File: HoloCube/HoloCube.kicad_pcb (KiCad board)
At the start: 4 copper layers, 30 x 29 mm, 38 parts, among them J1 ESPProgUART_RX, J2 Conn_01x08_MountingPin, J3 USB_C_Receptacle_USB2.0, J4 Micro_SD_Card, Q1 MMBT3904, U1 ESP32-PICO-D4, U2 LIS2DH12TR, U3 BH1750FVI-TR, U4 XC6209

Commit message: V0.1 FinalVer
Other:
- board text added: "JLCJLCJLCJLC"
- board text added: "KisonHe"
- board text added: "V0.1"
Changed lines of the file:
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@@
       (outputformat 1)
       (mirror false)
-      (drillshape 1)
+      (drillshape 0)
       (scaleselection 1)
-      (outputdirectory "")
+      (outputdirectory "plot/")
     )
   )
@@
     (fp_line (start 3.5 3.5) (end -3.5 3.5) (layer "F.Fab") (width 0.1))
     (fp_line (start -3.5 -2.5) (end -2.5 -3.5) (layer "F.Fab") (width 0.1))
-    (pad "" smd roundrect (at -0.66 -0.66) (size 1.07 1.07) (layers "F.Paste") (roundrect_rratio 0.233645))
-    (pad "" smd roundrect (at -1.98 -0.66) (size 1.07 1.07) (layers "F.Paste") (roundrect_rratio 0.233645))
-    (pad "" smd roundrect (at -0.66 1.98) (size 1.07 1.07) (layers "F.Paste") (roundrect_rratio 0.233645))
-    (pad "" smd roundrect (at 1.98 -1.98) (size 1.07 1.07) (layers "F.Paste") (roundrect_rratio 0.233645))
-    (pad "" smd roundrect (at 0.66 -1.98) (size 1.07 1.07) (layers "F.Paste") (roundrect_rratio 0.233645))
-    (pad "" smd roundrect (at 0.66 0.66) (size 1.07 1.07) (layers "F.Paste") (roundrect_rratio 0.233645))
-    (pad "" smd roundrect (at 1.98 -0.66) (size 1.07 1.07) (layers "F.Paste") (roundrect_rratio 0.233645))
-    (pad "" smd roundrect (at -1.98 0.66) (size 1.07 1.07) (layers "F.Paste") (roundrect_rratio 0.233645))
-    (pad "" smd roundrect (at -1.98 -1.98) (size 1.07 1.07) (layers "F.Paste") (roundrect_rratio 0.233645))
-    (pad "" smd roundrect (at 1.98 0.66) (size 1.07 1.07) (layers "F.Paste") (roundrect_rratio 0.233645))
-    (pad "" smd roundrect (at -1.98 1.98) (size 1.07 1.07) (layers "F.Paste") (roundrect_rratio 0.233645))
-    (pad "" smd roundrect (at -0.66 0.66) (size 1.07 1.07) (layers "F.Paste") (roundrect_rratio 0.233645))
-    (pad "" smd roundrect (at 1.98 1.98) (size 1.07 1.07) (layers "F.Paste") (roundrect_rratio 0.233645))
-    (pad "" smd roundrect (at -0.66 -1.98) (size 1.07 1.07) (layers "F.Paste") (roundrect_rratio 0.233645))
-    (pad "" smd roundrect (at 0.66 -0.66) (size 1.07 1.07) (layers "F.Paste") (roundrect_rratio 0.233645))
-    (pad "" smd roundrect (at 0.66 1.98) (size 1.07 1.07) (layers "F.Paste") (roundrect_rratio 0.233645))
+    (pad "" smd roundrect (at -0.66 -0.66) (size 1.07 1.07) (layers "F.Paste") (roundrect_rratio 0.2336448598))
+    (pad "" smd roundrect (at -1.98 -0.66) (size 1.07 1.07) (layers "F.Paste") (roundrect_rratio 0.2336448598))
+    (pad "" smd roundrect (at -0.66 1.98) (size 1.07 1.07) (layers "F.Paste") (roundrect_rratio 0.2336448598))
+    (pad "" smd roundrect (at 1.98 -1.98) (size 1.07 1.07) (layers "F.Paste") (roundrect_rratio 0.2336448598))
+    (pad "" smd roundrect (at 0.66 -1.98) (size 1.07 1.07) (layers "F.Paste") (roundrect_rratio 0.2336448598))
+    (pad "" smd roundrect (at 0.66 0.66) (size 1.07 1.07) (layers "F.Paste") (roundrect_rratio 0.2336448598))
+    (pad "" smd roundrect (at 1.98 -0.66) (size 1.07 1.07) (layers "F.Paste") (roundrect_rratio 0.2336448598))
+    (pad "" smd roundrect (at -1.98 0.66) (size 1.07 1.07) (layers "F.Paste") (roundrect_rratio 0.2336448598))
+    (pad "" smd roundrect (at -1.98 -1.98) (size 1.07 1.07) (layers "F.Paste") (roundrect_rratio 0.2336448598))
+    (pad "" smd roundrect (at 1.98 0.66) (size 1.07 1.07) (layers "F.Paste") (roundrect_rratio 0.2336448598))
+    (pad "" smd roundrect (at -1.98 1.98) (size 1.07 1.07) (layers "F.Paste") (roundrect_rratio 0.2336448598))
+    (pad "" smd roundrect (at -0.66 0.66) (size 1.07 1.07) (layers "F.Paste") (roundrect_rratio 0.2336448598))
+    (pad "" smd roundrect (at 1.98 1.98) (size 1.07 1.07) (layers "F.Paste") (roundrect_rratio 0.2336448598))
+    (pad "" smd roundrect (at -0.66 -1.98) (size 1.07 1.07) (layers "F.Paste") (roundrect_rratio 0.2336448598))
+    (pad "" smd roundrect (at 0.66 -0.66) (size 1.07 1.07) (layers "F.Paste") (roundrect_rratio 0.2336448598))
+    (pad "" smd roundrect (at 0.66 1.98) (size 1.07 1.07) (layers "F.Paste") (roundrect_rratio 0.2336448598))
     (pad "1" smd roundrect (at -3.45 -2.75) (size 0.8 0.25) (layers "F.Cu" "F.Paste" "F.Mask") (roundrect_rratio 0.25)
       (net 8 "+3V3") (pinfunction "VDDA") (pintype "power_in"))
@@
   (gr_arc (start 193.07 102.29) (mid 193.50934 101.22934) (end 194.57 100.79) (layer "Edge.Cuts") (width 0.1))
   (gr_line (start 221.57 100.79) (end 194.57 100.79) (layer "Edge.Cuts") (width 0.1))
+  (gr_text "V0.1" (at 194.87 103.42 90) (layer "B.SilkS")
+    (effects (font (size 1 1) (thickness 0.15)) (justify mirror))
+  )
+  (gr_text "KisonHe" (at 196.3 104.85 90) (layer "B.SilkS")
+    (effects (font (size 1 1) (thickness 0.15)) (justify mirror))
+  )
+  (gr_text "JLCJLCJLCJLC" (at 212.49 116.95 90) (layer "B.SilkS")
+    (effects (font (size 1 1) (thickness 0.15)) (justify mirror))
+  )
   (gr_text "这边是屁股，记得机械在光传感器上留出透明位置" (at 208.71 134.04) (layer "Cmts.User")
     (effects (font (size 1 1) (thickness 0.15)))

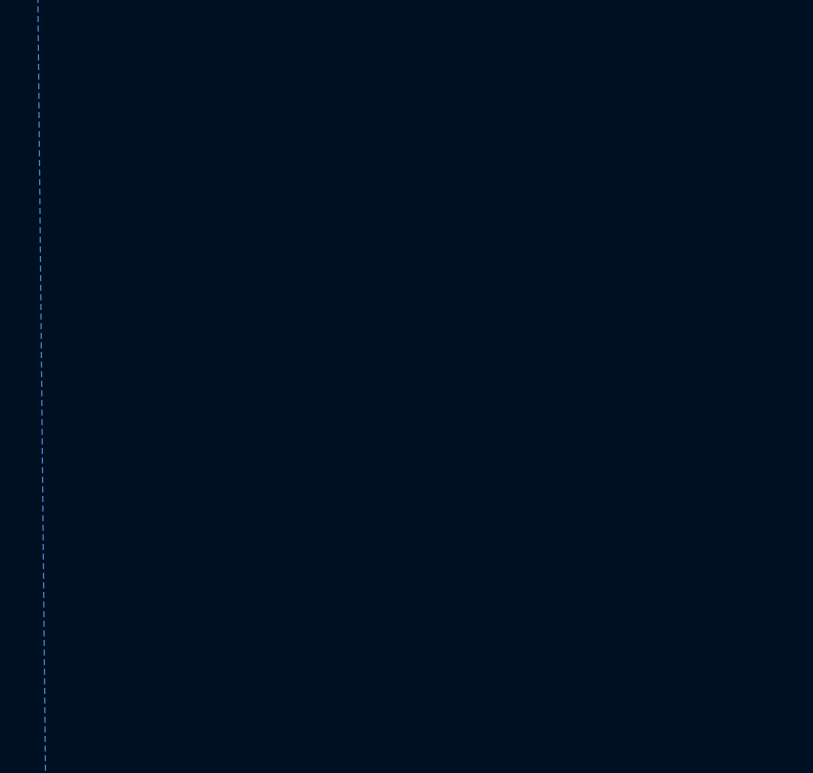
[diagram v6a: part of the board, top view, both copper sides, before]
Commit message: 只用三轴还是不方便输入，考虑增加波轮
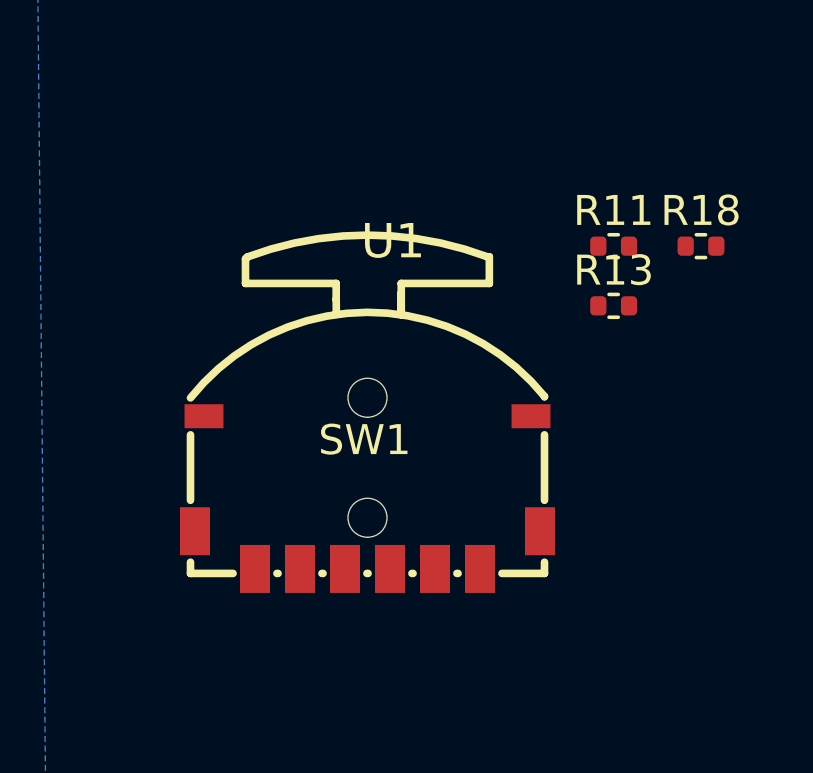
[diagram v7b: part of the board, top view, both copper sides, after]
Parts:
- added R11: 10k, Resistor_SMD:R_0402_1005Metric, F.Cu at (245.8, 125.2)
- added R13: 10k, Resistor_SMD:R_0402_1005Metric, F.Cu at (245.8, 127.2)
- added R18: 10k, Resistor_SMD:R_0402_1005Metric, F.Cu at (248.7, 125.2)
- added SW1: C318960, KisonNew:C318960, F.Cu at (237.5, 132.2)
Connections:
- AE1 pad 2: GND -> (no net)
- U1 pad 10: unconnected-(U1-Pad10) -> /IO34
- U1 pad 11: unconnected-(U1-Pad11) -> /IO35
- U1 pad 42: unconnected-(U1-Pad42) -> /IO21

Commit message: Fix  Error & add SW
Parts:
- removed R11, R13, R18: 10k, Resistor_SMD:R_0402_1005Metric
- removed R2: 0, Resistor_SMD:R_0402_1005Metric
- removed SW1: C318960, KisonNew:C318960
- J2: value Conn_01x08_MountingPin -> Conn_01x12_MountingPin; footprint Connector_FFC-FPC:TE_0-1734839-8_1x08-1MP_P0.5mm_Horizontal -> Connector_FFC-FPC:Hirose_FH12-12S-0.5SH_1x12-1MP_P0.50mm_Horizontal
- moved R14 1.60 mm to (220.7, 122.1)
- moved J2 0.96 mm to (217.6, 115.2)
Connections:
- J1 pad 2: Net-(J1-Pad2) -> +3V3
- U1 pad 16: /IO27 -> /BTN_Right
- U1 pad 17: /TMS -> /BTN_Left
- U1 pad 18: /IO12 -> unconnected-(U1-Pad18)
- U1 pad 42: /IO21 -> /BTN_Down
- U2 pad 6: unconnected-(U2-Pad6) -> GND
- U2 pad 7: unconnected-(U2-Pad7) -> GND
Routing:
- net /BTN_Right: track 0.00 -> 34.1 mm, vias 0 -> 2
- net /BTN_Down: track 0.00 -> 20.0 mm, vias 0 -> 2
- net /BTN_Left: track 0.00 -> 19.1 mm, vias 0 -> 2
- net +3V3: track 132.9 -> 141.5 mm
- net GND: track 31.4 -> 23.6 mm, vias 27 -> 29
- net Net-(J1-Pad2): track 5.56 -> 0.00 mm
- net /IO15: track 21.2 -> 23.8 mm
- net /IO22: track 20.0 -> 21.8 mm
- net /IO5: track 3.73 -> 5.37 mm
- net /IO18: track 3.73 -> 5.13 mm
- net /DC: track 3.73 -> 5.07 mm
- net /IO4: track 6.45 -> 5.13 mm
- net +5V: track 76.6 -> 75.4 mm
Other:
- board text added: "V0.2"
- board text removed: "V0.1"
